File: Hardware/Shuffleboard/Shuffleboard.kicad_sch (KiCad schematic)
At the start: 4 parts

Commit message: led's, mux
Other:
- sheet 8fig renamed 7Seg
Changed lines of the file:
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@@
 			(color 0 0 0 0.0000)
 		)
-		(property "Sheetname" "8fig"
+		(property "Sheetname" "7Seg"
 			(at 182.88 28.4984 0)
 			(effects

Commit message: fet led driving
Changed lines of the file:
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@@
 	(symbol
 		(lib_id "power:GND")
-		(at 78.74 41.91 90)
+		(at 77.47 41.91 90)
 		(unit 1)
 		(exclude_from_sim no)
@@
 		(fields_autoplaced yes)
 		(property "Reference" "#PWR01"
-			(at 85.09 41.91 0)
+			(at 83.82 41.91 0)
 			(effects
 				(font
@@
 		)
 		(property "Value" "GND"
-			(at 82.55 41.9099 90)
+			(at 81.28 41.9099 90)
 			(effects
 				(font
@@
 		)
 		(property "Footprint" ""
-			(at 78.74 41.91 0)
+			(at 77.47 41.91 0)
 			(effects
 				(font
@@
 		)
 		(property "Datasheet" ""
-			(at 78.74 41.91 0)
+			(at 77.47 41.91 0)
 			(effects
 				(font
@@
 		)
 		(property "Description" "Power symbol creates a global label with name \"GND\" , ground"
-			(at 78.74 41.91 0)
+			(at 77.47 41.91 0)
 			(effects
 				(font

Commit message: fet driving
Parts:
- added H5, H6: MountingHole, MountingHole:MountingHole_2.2mm_M2, symbol Mechanical:MountingHole
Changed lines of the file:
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@@
+	(symbol
+		(lib_id "Mechanical:MountingHole")
+		(at 246.38 59.69 0)
+		(unit 1)
+		(exclude_from_sim no)
+		(in_bom no)
+		(on_board yes)
+		(dnp no)
+		(fields_autoplaced yes)
+		(property "Reference" "H5"
+			(at 248.92 58.4199 0)
+			(effects
+				(font
+					(size 1.27 1.27)
+				)
+				(justify left)
+			)
+		)
+		(property "Value" "MountingHole"
+			(at 248.92 60.9599 0)
+			(effects
+				(font
+					(size 1.27 1.27)
+				)
+				(justify left)
+			)
+		)
+		(property "Footprint" "MountingHole:MountingHole_2.2mm_M2"
+			(at 246.38 59.69 0)
+			(effects
+				(font
+					(size 1.27 1.27)
+				)
+				(hide yes)
+			)
+		)
+		(property "Datasheet" "~"
+			(at 246.38 59.69 0)
+			(effects
+				(font
+					(size 1.27 1.27)
+				)
+				(hide yes)
+			)
+		)
+		(property "Description" "Mounting Hole without connection"
+			(at 246.38 59.69 0)
+			(effects
+				(font
+					(size 1.27 1.27)
+				)
+				(hide yes)
+			)
+		)
+		(instances
+			(project "Shuffleboard"
+				(path "/8d05e546-da1a-40d0-9e47-08c4b800bb0e"
+					(reference "H5")
+					(unit 1)
+				)
+			)
+		)
+	)
 	(symbol
 		(lib_id "Mechanical:MountingHole")
@@
 					(unit 1)
 				)
+			)
+		)
+	)
+	(symbol
+		(lib_id "Mechanical:MountingHole")
+		(at 246.38 66.04 0)
+		(unit 1)
+		(exclude_from_sim no)
+		(in_bom no)
+		(on_board yes)
+		(dnp no)
+		(fields_autoplaced yes)
+		(property "Reference" "H6"
+			(at 248.92 64.7699 0)
+			(effects
+				(font
+					(size 1.27 1.27)
+				)
+				(justify left)
+			)
+		)
+		(property "Value" "MountingHole"
+			(at 248.92 67.3099 0)
+			(effects
+				(font
+					(size 1.27 1.27)
+				)
+				(justify left)
+			)
+		)
+		(property "Footprint" "MountingHole:MountingHole_2.2mm_M2"
+			(at 246.38 66.04 0)
+			(effects
+				(font
+					(size 1.27 1.27)
+				)
+				(hide yes)
+			)
+		)
+		(property "Datasheet" "~"
+			(at 246.38 66.04 0)
+			(effects
+				(font
+					(size 1.27 1.27)
+				)
+				(hide yes)
+			)
+		)
+		(property "Description" "Mounting Hole without connection"
+			(at 246.38 66.04 0)
+			(effects
+				(font
+					(size 1.27 1.27)
+				)
+				(hide yes)
+			)
+		)
+		(instances
+			(project "Shuffleboard"
+				(path "/8d05e546-da1a-40d0-9e47-08c4b800bb0e"
+					(reference "H6")
+					(unit 1)
+				)

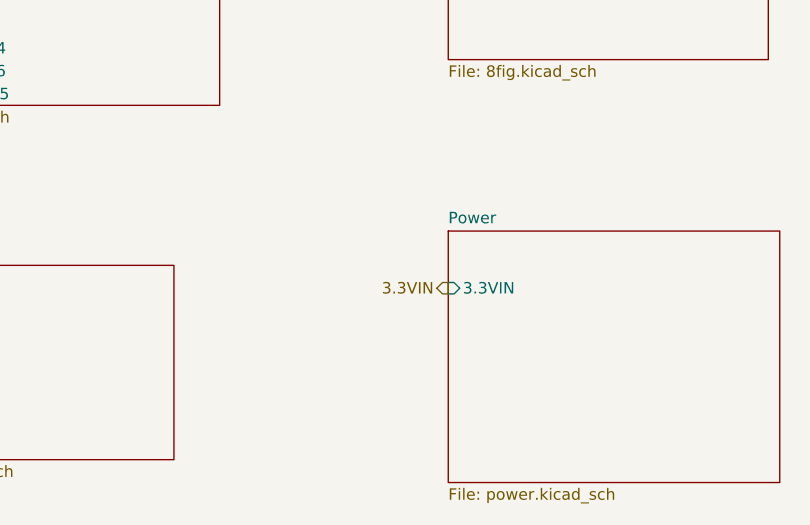
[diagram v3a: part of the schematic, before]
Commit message: series gate resistor
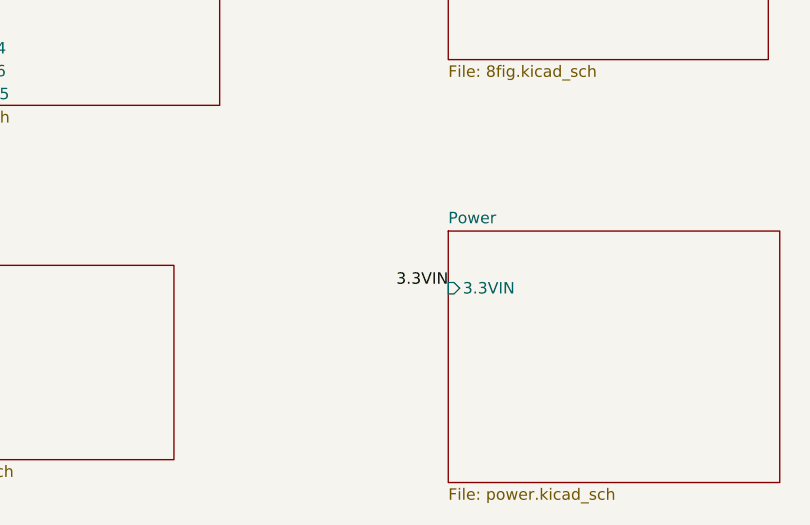
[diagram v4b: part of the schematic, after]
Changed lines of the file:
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@@
+	)
+	(label "3.3VIN"
+		(at 182.88 73.66 180)
+		(effects
+			(font
+				(size 1.27 1.27)
+			)
+			(justify right bottom)
+		)
 	)
 	(label "3.3VIN"
@@
 		)
 	)
-	(hierarchical_label "3.3VIN"
-		(shape output)
-		(at 182.88 73.66 180)
-		(effects
-			(font
-				(size 1.27 1.27)
-			)
-			(justify right)
-		)
-	)

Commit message: layout
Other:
- sheet 7Seg ports: added PB16_LATCH_PULSE, PB8_MOSI(PICO), PB9_SPI_CLK; removed none
- sheet Connector ports: added PB16_LATCH_PULSE, PB8_MOSI(PICO), PB9_SPI_CLK; removed none
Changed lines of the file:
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@@
+		)
+	)
+	(label "PB8_MOSI"
+		(at 182.88 38.1 180)
+		(effects
+			(font
+				(size 1.27 1.27)
+			)
+			(justify right bottom)
 		)
 	)
@@
 		)
 	)
+	(label "PB16_L{slash}P"
+		(at 182.88 40.64 180)
+		(effects
+			(font
+				(size 1.27 1.27)
+			)
+			(justify right bottom)
+		)
+	)
 	(label "3.3VIN"
 		(at 77.47 38.1 0)
@@
 		)
 	)
+	(label "PB8_MOSI"
+		(at 29.21 38.1 180)
+		(effects
+			(font
+				(size 1.27 1.27)
+			)
+			(justify right bottom)
+		)
+	)
 	(label "DACOut"
 		(at 77.47 45.72 0)
@@
 		)
 	)
+	(label "PB16_L{slash}P"
+		(at 29.21 33.02 180)
+		(effects
+			(font
+				(size 1.27 1.27)
+			)
+			(justify right bottom)
+		)
+	)
 	(label "PB1RST"
 		(at 29.21 54.61 180)
@@
 		)
 	)
+	(label "PB9_SPI_CLK"
+		(at 182.88 35.56 180)
+		(effects
+			(font
+				(size 1.27 1.27)
+			)
+			(justify right bottom)
+		)
+	)
 	(label "PB1RST"
 		(at 157.48 34.29 0)
@@
 			)
 			(justify left bottom)
+		)
+	)
+	(label "PB9_SPI_CLK"
+		(at 29.21 35.56 180)
+		(effects
+			(font
+				(size 1.27 1.27)
+			)
+			(justify right bottom)
 		)
 	)
@@
 			)
 		)
+		(pin "PB9_SPI_CLK" input
+			(at 182.88 35.56 180)
+			(effects
+				(font
+					(size 1.27 1.27)
+				)
+				(justify left)
+			)
+		)
+		(pin "PB8_MOSI(PICO)" input
+			(at 182.88 38.1 180)
+			(effects
+				(font
+					(size 1.27 1.27)
+				)
+				(justify left)
+			)
+		)
+		(pin "PB16_LATCH_PULSE" input
+			(at 182.88 40.64 180)
+			(effects
+				(font
+					(size 1.27 1.27)
+				)
+				(justify left)
+			)
+		)
 		(instances
 			(project "Shuffleboard"
@@
 			(effects
 				(font
+					(size 1.27 1.27)
+				)
+				(justify left)
+			)
+		)
+		(pin "PB8_MOSI(PICO)" output
+			(at 29.21 38.1 180)
+			(effects
+				(font
+					(size 1.27 1.27)
+				)
+				(justify left)
+			)
+		)
+		(pin "PB9_SPI_CLK" output
+			(at 29.21 35.56 180)
+			(effects
+				(font
+					(size 1.27 1.27)
+				)
+				(justify left)
+			)
+		)
+		(pin "PB16_LATCH_PULSE" output
+			(at 29.21 33.02 180)
+			(effects
+				(font

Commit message: layout 2
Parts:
- H1, H2, H3, H4, H5, H6: footprint MountingHole:MountingHole_2.2mm_M2 -> MountingHole:MountingHole_2.2mm_M2_DIN965_Pad
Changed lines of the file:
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@@
 			)
 		)
-		(property "Footprint" "MountingHole:MountingHole_2.2mm_M2"
+		(property "Footprint" "MountingHole:MountingHole_2.2mm_M2_DIN965_Pad"
 			(at 246.38 34.29 0)
 			(effects
@@
 			)
 		)
-		(property "Footprint" "MountingHole:MountingHole_2.2mm_M2"
+		(property "Footprint" "MountingHole:MountingHole_2.2mm_M2_DIN965_Pad"
 			(at 246.38 40.64 0)
 			(effects
@@
 			)
 		)
-		(property "Footprint" "MountingHole:MountingHole_2.2mm_M2"
+		(property "Footprint" "MountingHole:MountingHole_2.2mm_M2_DIN965_Pad"
 			(at 246.38 59.69 0)
 			(effects
@@
 			)
 		)
-		(property "Footprint" "MountingHole:MountingHole_2.2mm_M2"
+		(property "Footprint" "MountingHole:MountingHole_2.2mm_M2_DIN965_Pad"
 			(at 246.38 46.99 0)
 			(effects
@@
 			)
 		)
-		(property "Footprint" "MountingHole:MountingHole_2.2mm_M2"
+		(property "Footprint" "MountingHole:MountingHole_2.2mm_M2_DIN965_Pad"
 			(at 246.38 53.34 0)
 			(effects
@@
 			)
 		)
-		(property "Footprint" "MountingHole:MountingHole_2.2mm_M2"
+		(property "Footprint" "MountingHole:MountingHole_2.2mm_M2_DIN965_Pad"
 			(at 246.38 66.04 0)
 			(effects

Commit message: Finished Screen
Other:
- sheet Connector ports: added PA13_DC, PB15_RESET, PB6_TFT_CS, PB7_MISO(POCI); removed none
- sheet Screen ports: added PA13_DC, PB15_RESET, PB6_TFT_CS, PB7_MISO(POCI), PB8_MOSI(PICO), PB9_SPI_CLK; removed none
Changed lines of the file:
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@@
+		)
+	)
+	(label "PB7_MISO"
+		(at 52.07 29.21 90)
+		(effects
+			(font
+				(size 1.27 1.27)
+			)
+			(justify left bottom)
+		)
+	)
+	(label "PB9_SPI_CLK"
+		(at 115.57 82.55 180)
+		(effects
+			(font
+				(size 1.27 1.27)
+			)
+			(justify right bottom)
+		)
+	)
+	(label "PB15_RESET"
+		(at 115.57 74.93 180)
+		(effects
+			(font
+				(size 1.27 1.27)
+			)
+			(justify right bottom)
 		)
 	)
@@
 		)
 	)
+	(label "PB15_RESET"
+		(at 59.69 29.21 90)
+		(effects
+			(font
+				(size 1.27 1.27)
+			)
+			(justify left bottom)
+		)
+	)
+	(label "PB6_CS"
+		(at 57.15 29.21 90)
+		(effects
+			(font
+				(size 1.27 1.27)
+			)
+			(justify left bottom)
+		)
+	)
 	(label "3.3VIN"
 		(at 182.88 73.66 180)
@@
 		)
 	)
+	(label "PA13_DC"
+		(at 115.57 77.47 180)
+		(effects
+			(font
+				(size 1.27 1.27)
+			)
+			(justify right bottom)
+		)
+	)
 	(label "PB16_L{slash}P"
 		(at 182.88 40.64 180)
@@
 		)
 	)
+	(label "PB6_CS"
+		(at 115.57 87.63 180)
+		(effects
+			(font
+				(size 1.27 1.27)
+			)
+			(justify right bottom)
+		)
+	)
 	(label "3.3VIN"
 		(at 77.47 38.1 0)
@@
 		)
 	)
+	(label "PB7_MISO"
+		(at 115.57 85.09 180)
+		(effects
+			(font
+				(size 1.27 1.27)
+			)
+			(justify right bottom)
+		)
+	)
+	(label "PA13_DC"
+		(at 54.61 29.21 90)
+		(effects
+			(font
+				(size 1.27 1.27)
+			)
+			(justify left bottom)
+		)
+	)
 	(label "PB1RST"
 		(at 29.21 54.61 180)
@@
 	(label "PB9_SPI_CLK"
 		(at 29.21 35.56 180)
+		(effects
+			(font
+				(size 1.27 1.27)
+			)
+			(justify right bottom)
+		)
+	)
+	(label "PB8_MOSI"
+		(at 115.57 80.01 180)
 		(effects
 			(font
@@
 			)
 		)
+		(pin "PB15_RESET" input
+			(at 115.57 74.93 180)
+			(effects
+				(font
+					(size 1.27 1.27)
+				)
+				(justify left)
+			)
+		)
+		(pin "PA13_DC" input
+			(at 115.57 77.47 180)
+			(effects
+				(font
+					(size 1.27 1.27)
+				)
+				(justify left)
+			)
+		)
+		(pin "PB8_MOSI(PICO)" input
+			(at 115.57 80.01 180)
+			(effects
+				(font
+					(size 1.27 1.27)
+				)
+				(justify left)
+			)
+		)
+		(pin "PB9_SPI_CLK" input
+			(at 115.57 82.55 180)
+			(effects
+				(font
+					(size 1.27 1.27)
+				)
+				(justify left)
+			)
+		)
+		(pin "PB7_MISO(POCI)" input
+			(at 115.57 85.09 180)
+			(effects
+				(font
+					(size 1.27 1.27)
+				)
+				(justify left)
+			)
+		)
+		(pin "PB6_TFT_CS" input
+			(at 115.57 87.63 180)
+			(effects
+				(font
+					(size 1.27 1.27)
+				)
+				(justify left)
+			)
+		)
 		(instances
 			(project "Shuffleboard"
@@
 			)
 		)
+		(pin "PB7_MISO(POCI)" output
+			(at 52.07 29.21 90)
+			(effects
+				(font
+					(size 1.27 1.27)
+				)
+				(justify right)
+			)
+		)
+		(pin "PA13_DC" output
+			(at 54.61 29.21 90)
+			(effects
+				(font
+					(size 1.27 1.27)
+				)
+				(justify right)
+			)
+		)
+		(pin "PB6_TFT_CS" output
+			(at 57.15 29.21 90)
+			(effects
+				(font
+					(size 1.27 1.27)
+				)
+				(justify right)
+			)
+		)
+		(pin "PB15_RESET" output
+			(at 59.69 29.21 90)
+			(effects
+				(font
+					(size 1.27 1.27)
+				)
+				(justify right)
+			)
+		)

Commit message: finished layout
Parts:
- H1, H2, H3, H4, H5, H6: value MountingHole -> (none)
